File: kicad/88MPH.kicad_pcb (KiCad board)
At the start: 2 copper layers, 102.9 x 31.8 mm, 27 parts, among them CON1 AVR-ISP-6, IC1 ATMEGA328P-P, P1 CONN_01X04, Q1 Q_NPN_EBC, Q2 Q_NPN_EBC

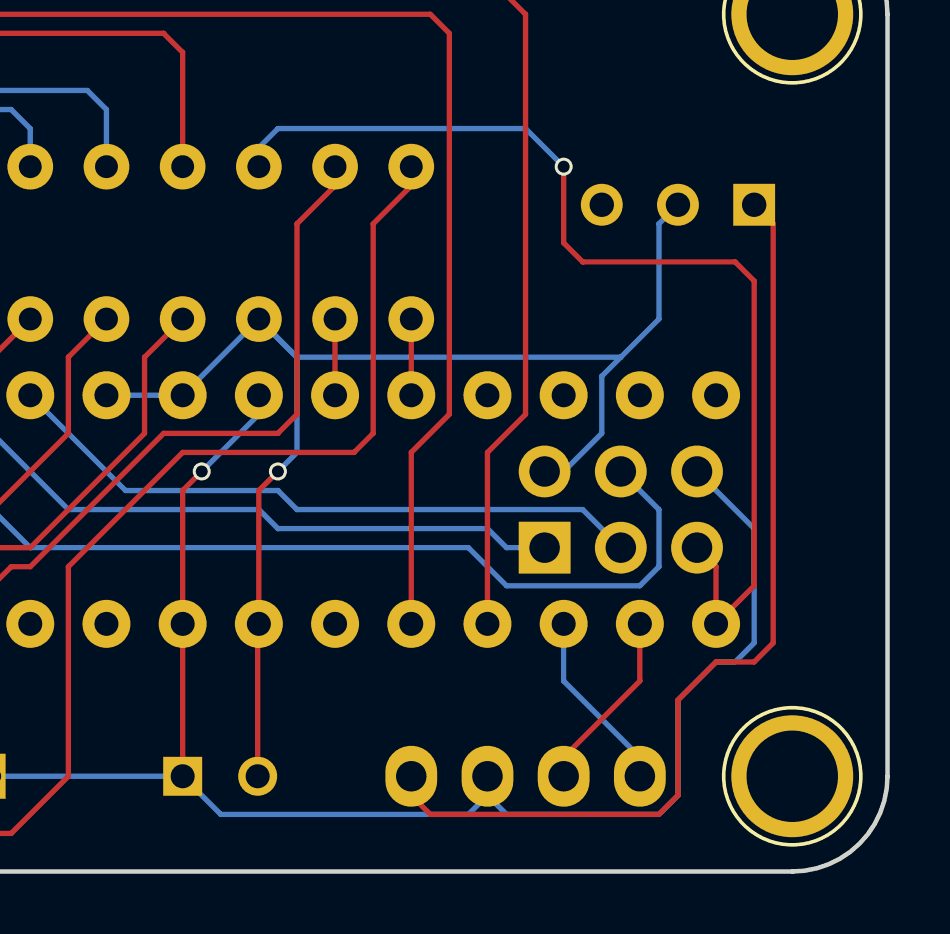
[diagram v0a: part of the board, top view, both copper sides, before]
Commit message: Cleanup of footprints and text
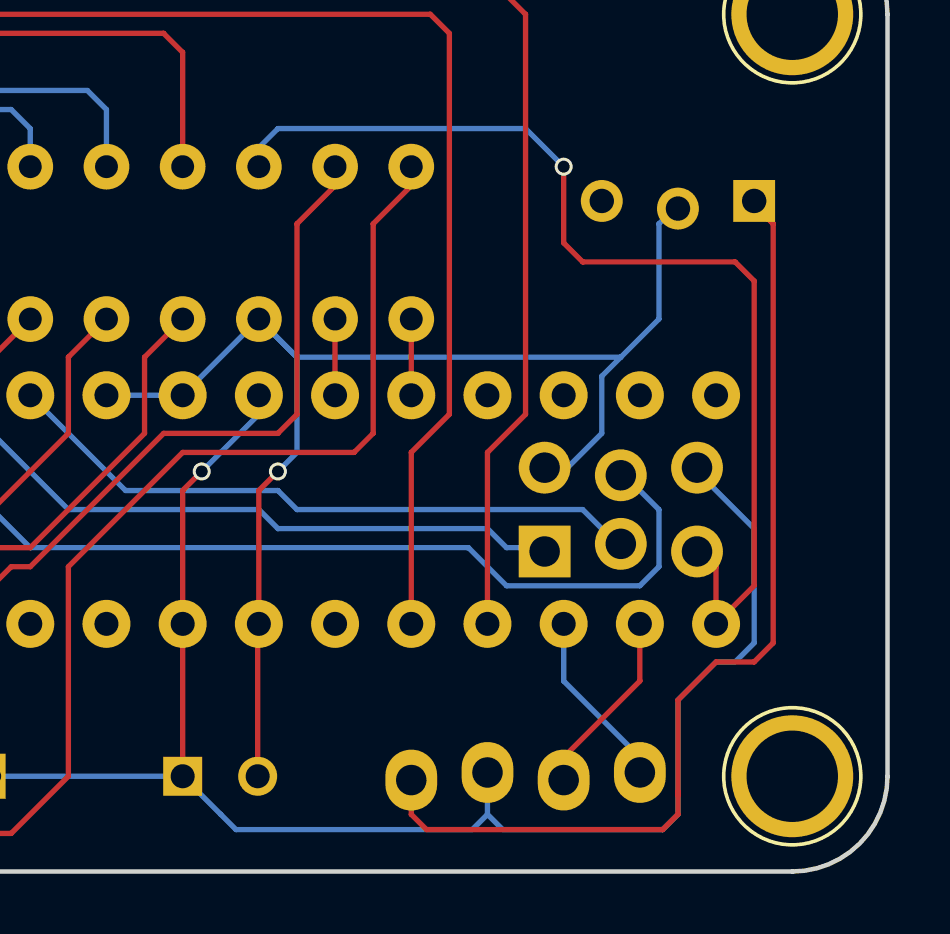
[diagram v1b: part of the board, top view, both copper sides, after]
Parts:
- PWR1: footprint Buttons_Switches_ThroughHole:SW_Micro_SPST -> misc:SW_Micro_SPST_Lock
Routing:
- net GND: track 136.9 -> 139.2 mm
- net VCC: track 33.0 -> 34.8 mm
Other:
- board text added: "BLK"
- board text added: "RED"
